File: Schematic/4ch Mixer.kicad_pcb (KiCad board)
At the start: 2 copper layers, 30 x 100 mm, 44 parts, among them P1 Power, U1 TL074, U2 TL072

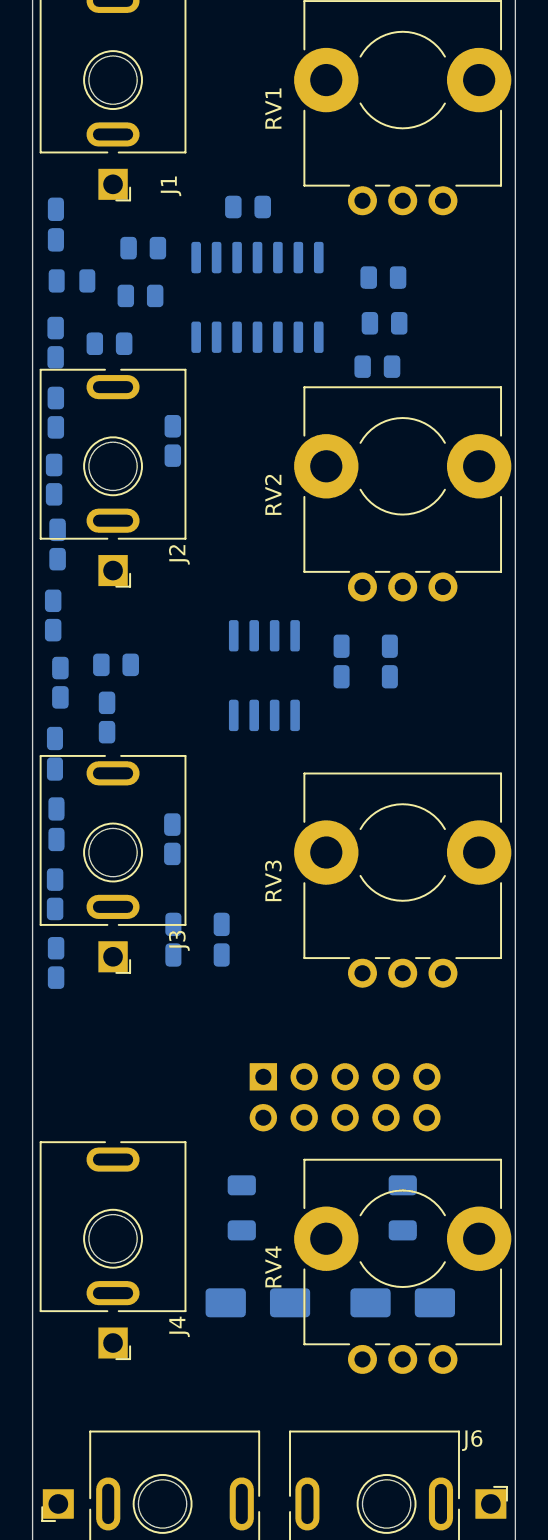
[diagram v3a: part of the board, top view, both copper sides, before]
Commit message: Optimise resistor and capacitor placement for short wires
anneal_place.py minimises total wire length (ground excluded, since it goes
to a pour; rails weighted lower) with 1 mm spacing for hand soldering. Fixes
the back-side transform in pcbgen: KiCad mirrors back parts and rotates them
by -rot, checked against the drill file. DRC: no errors.
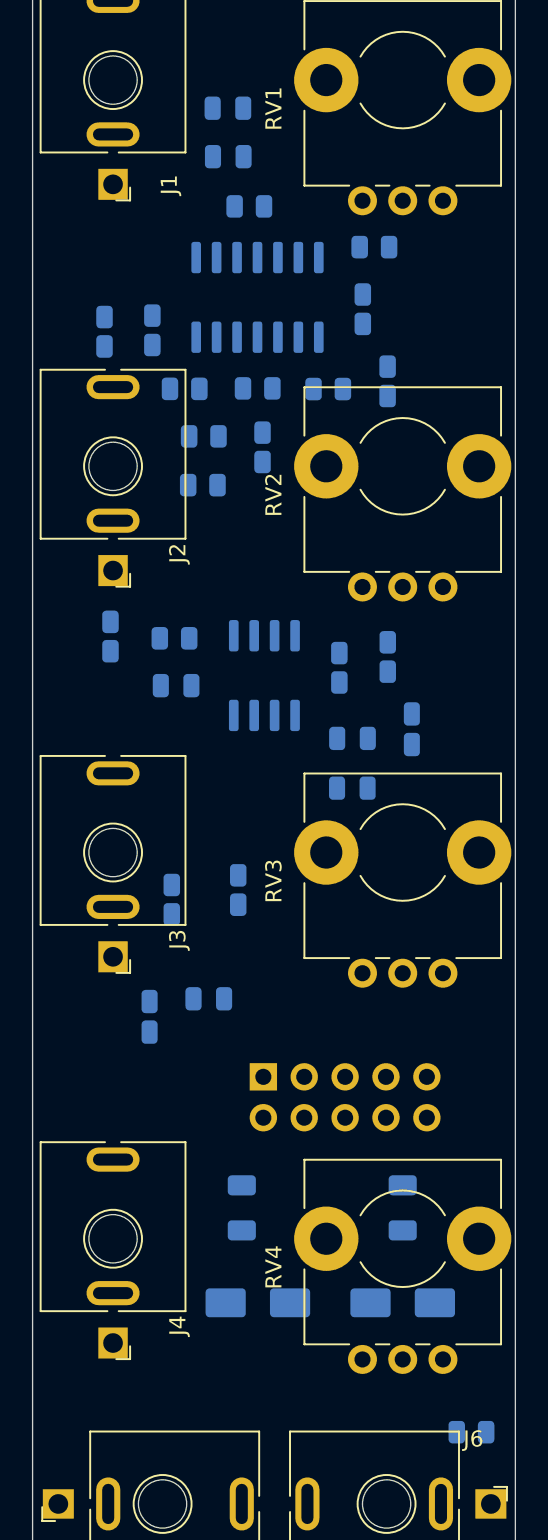
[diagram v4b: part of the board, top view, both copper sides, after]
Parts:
- moved R19 49.9 mm to (127.3, 140.5), turned to 0 degrees
- moved R15 22.6 mm to (119.1, 93.0)
- moved C7 22.2 mm to (123.6, 96.9)
- moved R14 21.0 mm to (122.1, 92.4)
- moved R3 16.2 mm to (122.1, 75.2), turned to 90 degrees
- moved R17 15.9 mm to (112.8, 106.8), turned to 90 degrees
- moved R4 14.4 mm to (114.3, 79.3), turned to 90 degrees
- moved R8 13.9 mm to (118.4, 75.7)
- moved C3 12.9 mm to (112.1, 58.3), turned to 0 degrees
- moved R7 12.9 mm to (114.0, 75.7), turned to 0 degrees
- moved R16 12.5 mm to (108.8, 91.2), turned to 0 degrees
- moved C4 12.4 mm to (112.2, 61.3)
- moved R2 12.0 mm to (109.5, 75.7)
- moved C8 11.4 mm to (108.9, 94.2), turned to 0 degrees
- moved R5 11.1 mm to (113.5, 64.4)
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
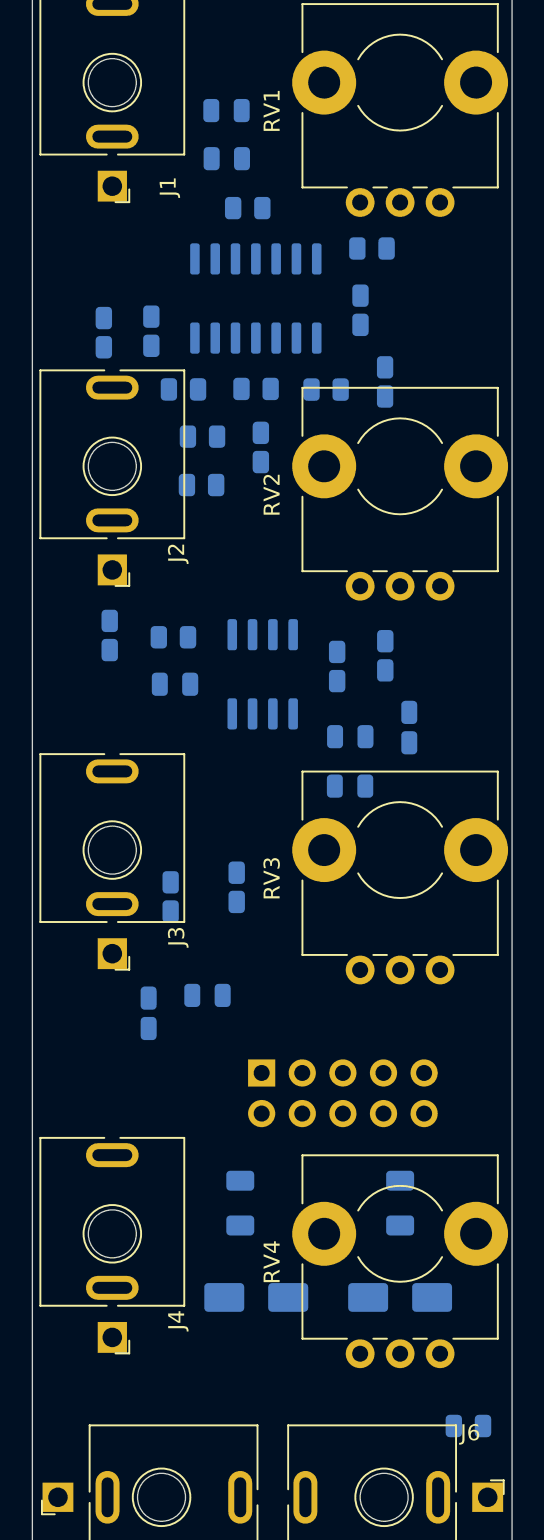
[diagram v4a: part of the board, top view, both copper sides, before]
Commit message: Keep resistors and capacitors at 0 degrees; fix pad angles in the generator
Rotated SMD parts had unrotated pad shapes: KiCad stores each pad's angle
including the part rotation, and the generator did not write it. The
generator now does, and the optimiser no longer rotates parts (default).
All resistors and capacitors are at 0 degrees. DRC: no errors.
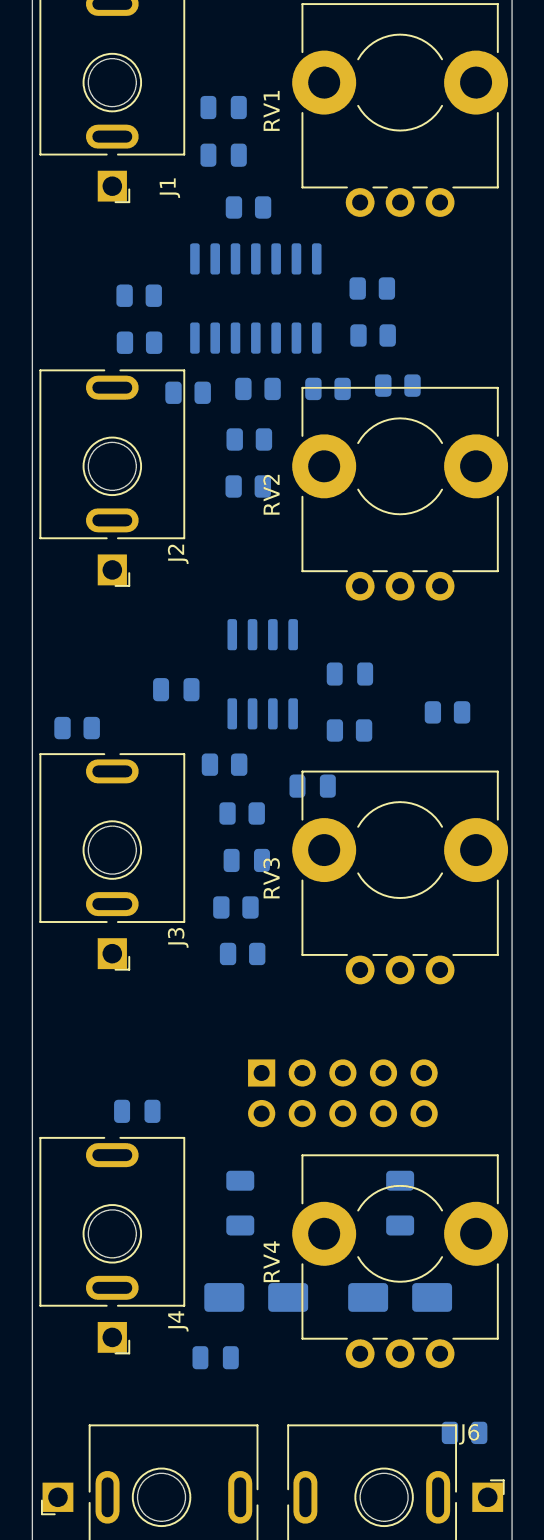
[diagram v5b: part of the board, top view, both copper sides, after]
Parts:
- moved R11 39.8 mm to (113.2, 111.0), turned to 0 degrees
- moved C5 21.9 mm to (111.5, 136.3), turned to 0 degrees
- moved R17 17.1 mm to (126.0, 95.9), turned to 0 degrees
- moved R15 16.3 mm to (112.7, 108.1), turned to 0 degrees
- moved R4 15.0 mm to (113.5, 64.3), turned to 0 degrees
- moved R13 13.9 mm to (113.1, 102.2), turned to 0 degrees
- moved R18 12.1 mm to (102.8, 96.9), turned to 0 degrees
- moved R6 10.7 mm to (113.6, 78.8), turned to 0 degrees
- moved C2 10.1 mm to (113.4, 105.2)
- moved R9 9.93 mm to (118.5, 75.7)
- moved R5 8.73 mm to (106.7, 69.8)
- moved R16 8.59 mm to (112.0, 99.2)
- moved C6 8.48 mm to (106.6, 120.9)
- moved R2 7.30 mm to (113.5, 81.8)
- moved R8 6.95 mm to (121.3, 69.4)
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
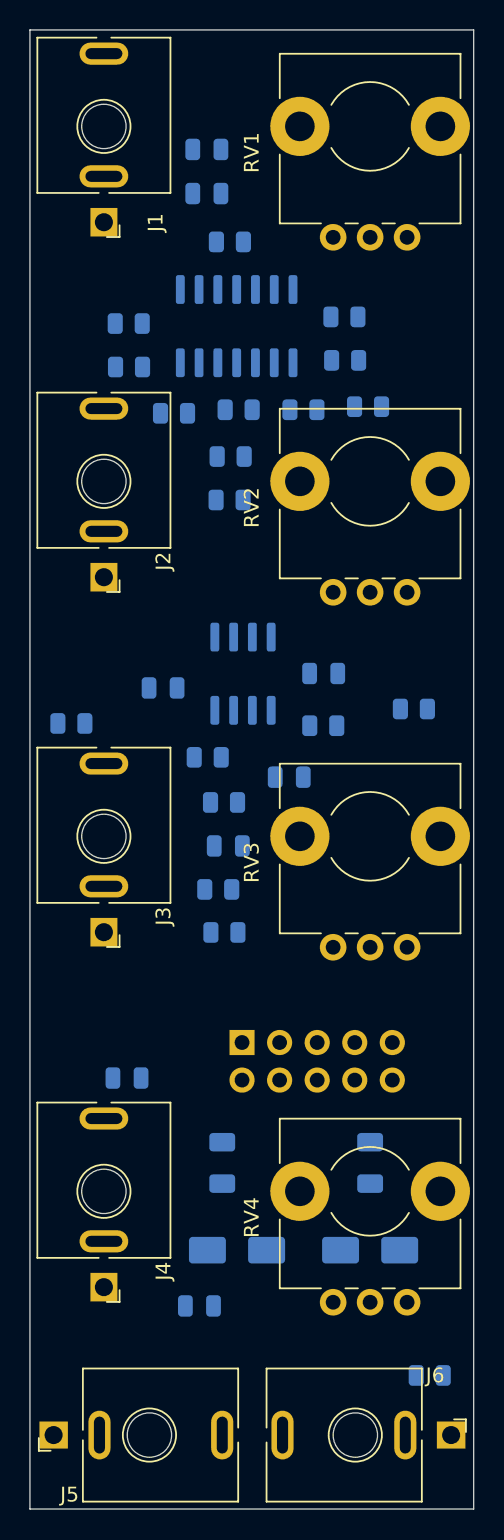
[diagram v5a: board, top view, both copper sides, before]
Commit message: Refill zones, align passive columns and spacing, place reference labels
Refilled the GNDA zones (stale fill caused the zone clearance errors),
snapped passive columns to a common x and evenly spaced each run, and
moved the back-side reference labels next to their parts. DRC: no errors
except the pot mounting pads near the board edge (pot placement, not
touched here) and some remaining label/silkscreen overlaps.
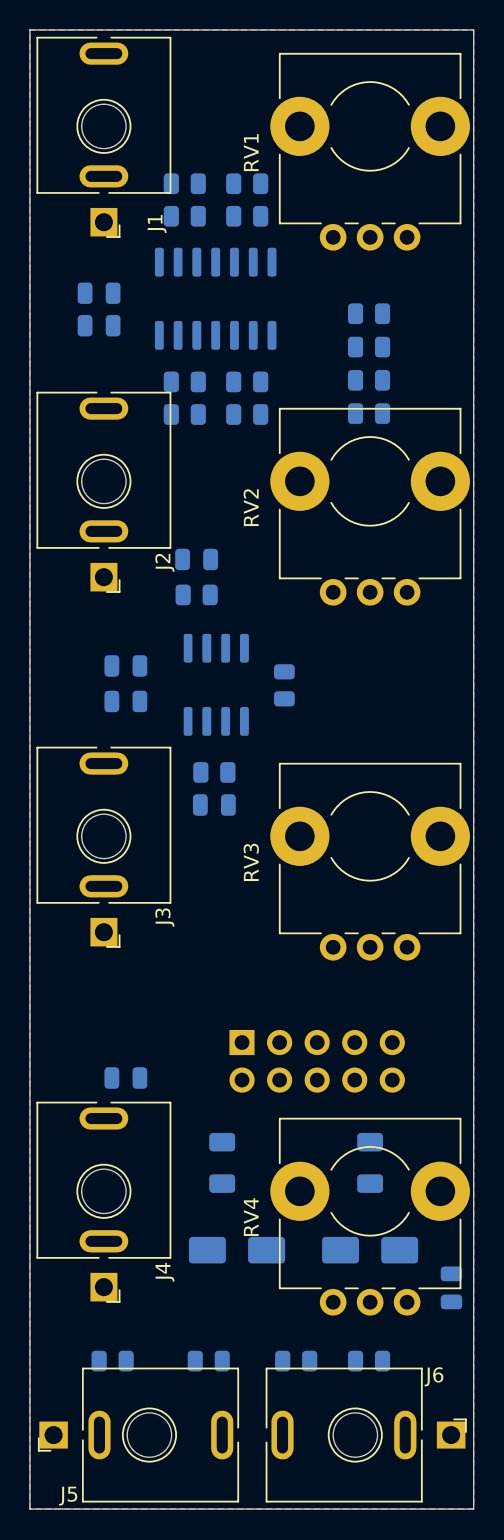
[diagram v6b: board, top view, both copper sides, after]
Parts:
- moved R17 44.2 mm to (122.9, 140.0)
- moved R18 44.1 mm to (112.1, 140.0), turned to 180 degrees
- moved R16 41.3 mm to (105.6, 140.0), turned to 180 degrees
- moved R11 38.6 mm to (122.9, 73.7), turned to 180 degrees
- moved R2 21.4 mm to (114.7, 60.4)
- moved C5 17.1 mm to (128.5, 135.1), turned to -90 degrees
- moved R12 16.5 mm to (122.9, 75.9), turned to 180 degrees
- moved R6 16.3 mm to (114.7, 62.6)
- moved R1 16.1 mm to (110.5, 60.4), turned to 180 degrees
- moved R10 14.8 mm to (122.9, 69.2), turned to 180 degrees
- moved R13 14.2 mm to (111.3, 88.2)
- moved C2 14.0 mm to (106.5, 93.0)
- moved C1 12.2 mm to (106.5, 95.4), turned to 180 degrees
- moved C3 12.1 mm to (104.7, 67.8), turned to 180 degrees
- moved R4 12.1 mm to (110.5, 76.0), turned to 180 degrees
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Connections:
- C1 pad 1: Net-(D1-K) -> +12VA
- C1 pad 2: Net-(C1-~-Pad2) -> GNDA
- C2 pad 1: Net-(C1-~-Pad2) -> GNDA
- C3 pad 2: Net-(C3-~-Pad2) -> GNDA
- C4 pad 1: Net-(C3-~-Pad2) -> GNDA
- C5 pad 1: Net-(D1-K) -> +12VA
- C5 pad 2: Net-(C5-~-Pad2) -> GNDA
- C6 pad 1: Net-(C5-~-Pad2) -> GNDA
- D1 pad 1: Net-(D1-K) -> +12VA
- D1 pad 2: Net-(D1-A) -> GNDA
- D2 pad 1: Net-(D1-A) -> GNDA
- F1 pad 2: Net-(D1-K) -> +12VA
- R10 pad 1: Net-(R10-~-Pad1) -> Net-(U2A--)
- R11 pad 1: Net-(R11-~-Pad1) -> Net-(U2A--)
- R12 pad 1: Net-(R10-~-Pad1) -> Net-(U2A--)
- R13 pad 2: Net-(R11-~-Pad1) -> Net-(U2A--)
- R9 pad 1: Net-(U1A-~) -> Net-(U2A--)
- R9 pad 2: Net-(R10-~-Pad1) -> Net-(U1A-~)
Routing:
- added copper zone on B.Cu, net GNDA
- added copper zone on F.Cu, net GNDA

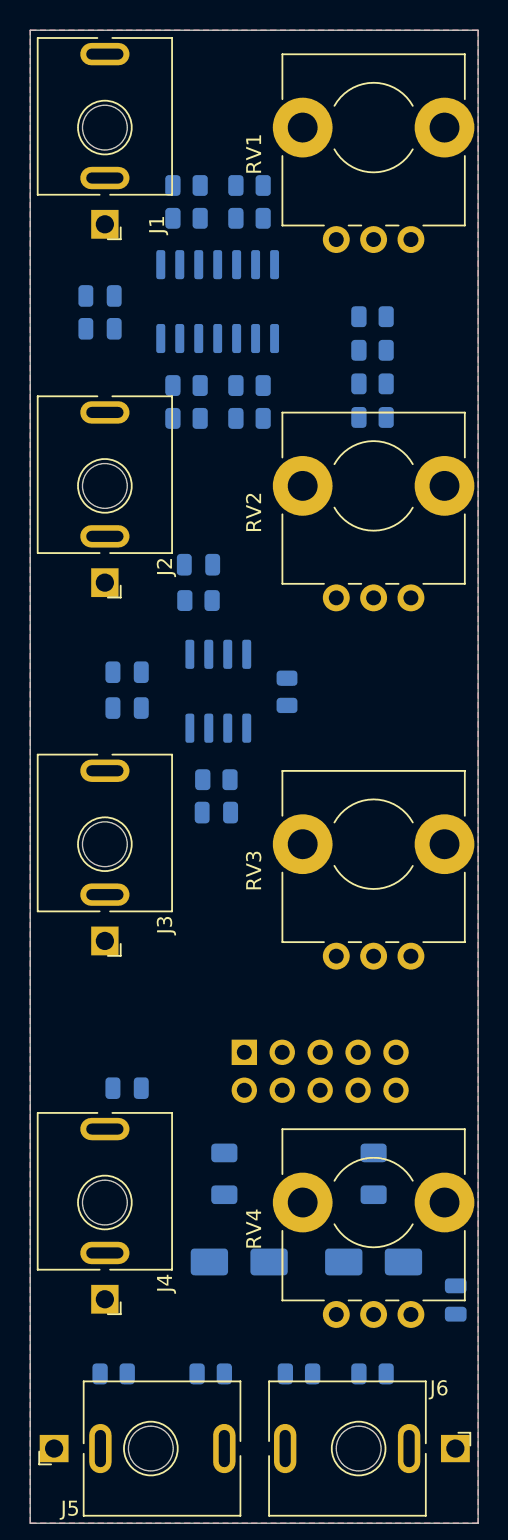
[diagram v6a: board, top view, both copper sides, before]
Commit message: Routed SMD board
Hand-arranged placement and routing from KiCad, with the schematic missing
connections fixed by hand. The jack footprint uses the Attenuverter's
orientation. DRC: no unconnected items; only the three accepted thermal
spoke warnings remain.
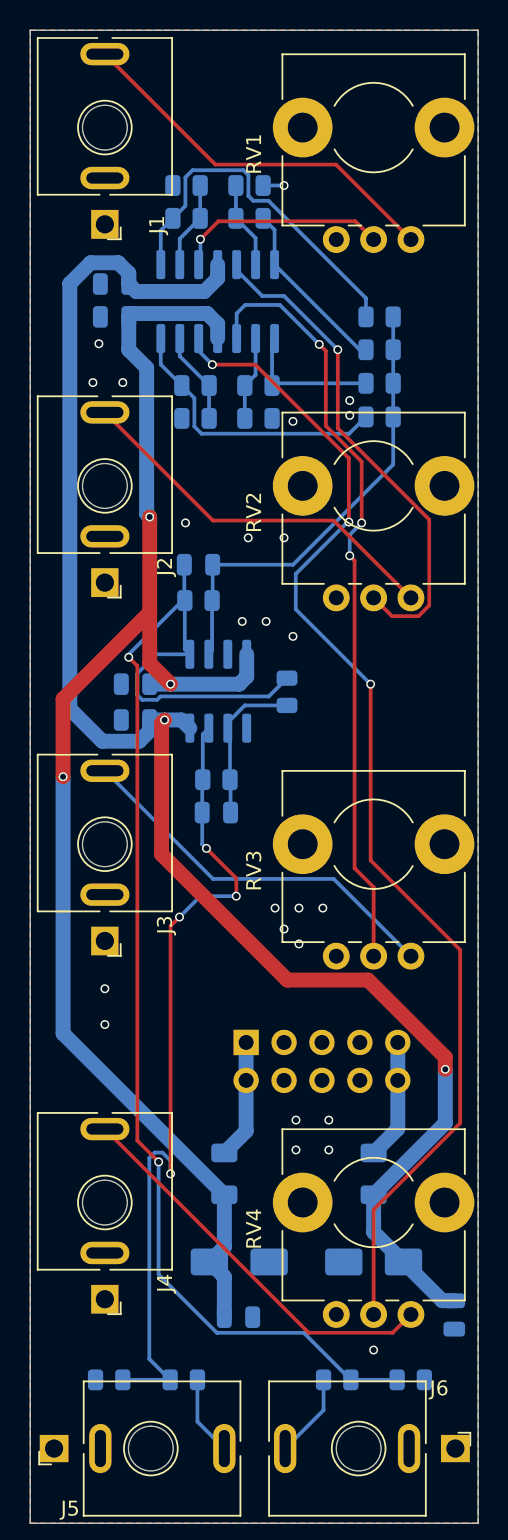
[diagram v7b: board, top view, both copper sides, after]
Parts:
- moved C6 17.1 mm to (114.0, 136.2), turned to 180 degrees
- moved R17 2.59 mm to (125.5, 140.4)
- moved R19 2.59 mm to (120.6, 140.4)
- moved R9 2.29 mm to (123.4, 69.2)
- moved R10 2.26 mm to (123.4, 71.4)
- moved R18 1.84 mm to (110.3, 140.4)
- moved C3 1.26 mm to (105.7, 67.0)
- moved C4 1.26 mm to (105.7, 69.2), turned to 0 degrees
- moved C5 1.00 mm to (128.4, 136.1)
- moved C1 0.98 mm to (107.0, 96.2)
- moved C2 0.98 mm to (107.0, 93.8)
- moved P1 0.67 mm to (114.5, 117.8)
- moved R4 0.60 mm to (111.1, 76.0)
- moved R8 0.60 mm to (111.1, 73.8)
- moved R3 0.60 mm to (115.3, 76.0)
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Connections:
- RV1 pad : (no net) -> GNDA
- RV2 pad : (no net) -> GNDA
- RV3 pad : (no net) -> GNDA
- RV4 pad : (no net) -> GNDA
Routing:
- net +12VA: track 0.00 -> 106.4 mm, vias 0 -> 2
- net -12VA: track 0.00 -> 96.2 mm, vias 0 -> 3
- net Net-(U2A-~): track 0.00 -> 89.3 mm, vias 0 -> 2
- net Net-(U1D-+): track 0.00 -> 80.0 mm, vias 0 -> 3
- net Net-(U2B-~): track 0.00 -> 55.5 mm, vias 0 -> 4
- net Net-(U1C-+): track 0.00 -> 51.7 mm, vias 0 -> 3
- net Net-(U1B-+): track 0.00 -> 33.6 mm, vias 0 -> 1
- net Net-(U2A--): track 0.00 -> 30.9 mm
- net Net-(J4-PadT): track 0.00 -> 26.7 mm
- net Net-(J3-PadT): track 0.00 -> 25.6 mm
- net Net-(J2-PadT): track 0.00 -> 25.6 mm
- net Net-(J1-PadT): track 0.00 -> 25.6 mm
- net Net-(U1A-~): track 0.00 -> 24.4 mm
- net Net-(U1D-~): track 0.00 -> 19.0 mm
- net Net-(U1A-+): track 0.00 -> 14.4 mm, vias 0 -> 1
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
